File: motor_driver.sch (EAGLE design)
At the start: 43 parts, among them IC1 LM2936DT-5.0, Q1 BC849SMD, Q10 IRLML5203, Q11 BC849SMD, Q2 BC849SMD, Q3 BC849SMD, Q4 BC849SMD, Q5 BC849SMD, Q6 BC849SMD, Q7 IRLML5203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

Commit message: changed resistors in m1, m2 drivers
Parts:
- R11, R12, R13, R14: device rcl:R-EU_R0603 -> rcl:R-EU_R2512
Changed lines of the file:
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@@
 <?xml version="1.0" encoding="utf-8"?>
 <!DOCTYPE eagle SYSTEM "eagle.dtd">
-<eagle version="7.1.0">
+<eagle version="7.2.0">
 <drawing>
 <settings>
@@
 <grid distance="0.1" unitdist="inch" unit="inch" style="lines" multiple="1" display="no" altdistance="0.01" altunitdist="inch" altunit="inch"/>
 <layers>
-<layer number="1" name="Top" color="4" fill="1" visible="no" active="no"/>
-<layer number="16" name="Bottom" color="1" fill="1" visible="no" active="no"/>
-<layer number="17" name="Pads" color="2" fill="1" visible="no" active="no"/>
-<layer number="18" name="Vias" color="2" fill="1" visible="no" active="no"/>
-<layer number="19" name="Unrouted" color="6" fill="1" visible="no" active="no"/>
-<layer number="20" name="Dimension" color="15" fill="1" visible="no" active="no"/>
-<layer number="21" name="tPlace" color="7" fill="1" visible="no" active="no"/>
-<layer number="22" name="bPlace" color="7" fill="1" visible="no" active="no"/>
-<layer number="23" name="tOrigins" color="15" fill="1" visible="no" active="no"/>
-<layer number="24" name="bOrigins" color="15" fill="1" visible="no" active="no"/>
-<layer number="25" name="tNames" color="7" fill="1" visible="no" active="no"/>
-<layer number="26" name="bNames" color="7" fill="1" visible="no" active="no"/>
-<layer number="27" name="tValues" color="7" fill="1" visible="no" active="no"/>
-<layer number="28" name="bValues" color="7" fill="1" visible="no" active="no"/>
+<layer number="1" name="Top" color="4" fill="1" visible="yes" active="no"/>
+<layer number="16" name="Bottom" color="1" fill="1" visible="yes" active="no"/>
+<layer number="17" name="Pads" color="2" fill="1" visible="yes" active="no"/>
+<layer number="18" name="Vias" color="2" fill="1" visible="yes" active="no"/>
+<layer number="19" name="Unrouted" color="6" fill="1" visible="yes" active="no"/>
+<layer number="20" name="Dimension" color="15" fill="1" visible="yes" active="no"/>
+<layer number="21" name="tPlace" color="7" fill="1" visible="yes" active="no"/>
+<layer number="22" name="bPlace" color="7" fill="1" visible="yes" active="no"/>
+<layer number="23" name="tOrigins" color="15" fill="1" visible="yes" active="no"/>
+<layer number="24" name="bOrigins" color="15" fill="1" visible="yes" active="no"/>
+<layer number="25" name="tNames" color="7" fill="1" visible="yes" active="no"/>
+<layer number="26" name="bNames" color="7" fill="1" visible="yes" active="no"/>
+<layer number="27" name="tValues" color="7" fill="1" visible="yes" active="no"/>
+<layer number="28" name="bValues" color="7" fill="1" visible="yes" active="no"/>
 <layer number="29" name="tStop" color="7" fill="3" visible="no" active="no"/>
 <layer number="30" name="bStop" color="7" fill="6" visible="no" active="no"/>
@@
 <layer number="35" name="tGlue" color="7" fill="4" visible="no" active="no"/>
 <layer number="36" name="bGlue" color="7" fill="5" visible="no" active="no"/>
-<layer number="37" name="tTest" color="7" fill="1" visible="no" active="no"/>
-<layer number="38" name="bTest" color="7" fill="1" visible="no" active="no"/>
+<layer number="37" name="tTest" color="7" fill="1" visible="yes" active="no"/>
+<layer number="38" name="bTest" color="7" fill="1" visible="yes" active="no"/>
 <layer number="39" name="tKeepout" color="4" fill="11" visible="no" active="no"/>
 <layer number="40" name="bKeepout" color="1" fill="11" visible="no" active="no"/>
@@
 <layer number="44" name="Drills" color="7" fill="1" visible="no" active="no"/>
 <layer number="45" name="Holes" color="7" fill="1" visible="no" active="no"/>
-<layer number="46" name="Milling" color="3" fill="1" visible="no" active="no"/>
-<layer number="47" name="Measures" color="7" fill="1" visible="no" active="no"/>
-<layer number="48" name="Document" color="7" fill="1" visible="no" active="no"/>
-<layer number="49" name="Reference" color="7" fill="1" visible="no" active="no"/>
-<layer number="51" name="tDocu" color="7" fill="1" visible="no" active="no"/>
-<layer number="52" name="bDocu" color="7" fill="1" visible="no" active="no"/>
+<layer number="46" name="Milling" color="3" fill="1" visible="yes" active="no"/>
+<layer number="47" name="Measures" color="7" fill="1" visible="yes" active="no"/>
+<layer number="48" name="Document" color="7" fill="1" visible="yes" active="no"/>
+<layer number="49" name="Reference" color="7" fill="1" visible="yes" active="no"/>
+<layer number="51" name="tDocu" color="7" fill="1" visible="yes" active="no"/>
+<layer number="52" name="bDocu" color="7" fill="1" visible="yes" active="no"/>
 <layer number="90" name="Modules" color="5" fill="1" visible="yes" active="yes"/>
 <layer number="91" name="Nets" color="2" fill="1" visible="yes" active="yes"/>
@@
 <part name="R10" library="rcl" deviceset="R-EU_" device="R0603" value="100k"/>
 <part name="R4" library="rcl" deviceset="R-EU_" device="R0603" value="10k"/>
-<part name="R14" library="rcl" deviceset="R-EU_" device="R0603" value="10"/>
-<part name="R12" library="rcl" deviceset="R-EU_" device="R0603" value="10"/>
+<part name="R14" library="rcl" deviceset="R-EU_" device="R2512" value="10"/>
+<part name="R12" library="rcl" deviceset="R-EU_" device="R2512" value="10"/>
 <part name="SUPPLY10" library="supply2" deviceset="VDD" device=""/>
 <part name="GND4" library="supply1" deviceset="GND" device=""/>
@@
 <part name="R9" library="rcl" deviceset="R-EU_" device="R0603" value="100k"/>
 <part name="R2" library="rcl" deviceset="R-EU_" device="R0603" value="10k"/>
-<part name="R13" library="rcl" deviceset="R-EU_" device="R0603" value="10"/>
-<part name="R11" library="rcl" deviceset="R-EU_" device="R0603" value="10"/>
+<part name="R13" library="rcl" deviceset="R-EU_" device="R2512" value="10"/>
+<part name="R11" library="rcl" deviceset="R-EU_" device="R2512" value="10"/>
 <part name="SUPPLY9" library="supply2" deviceset="VDD" device=""/>
 <part name="GND3" library="supply1" deviceset="GND" device=""/>

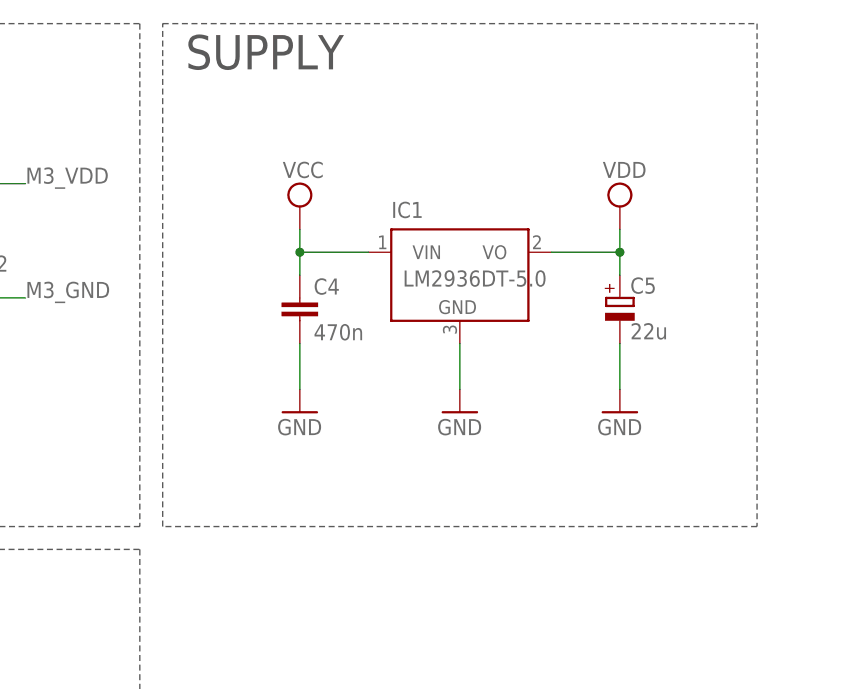
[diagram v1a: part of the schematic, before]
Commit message: added LED, added bom
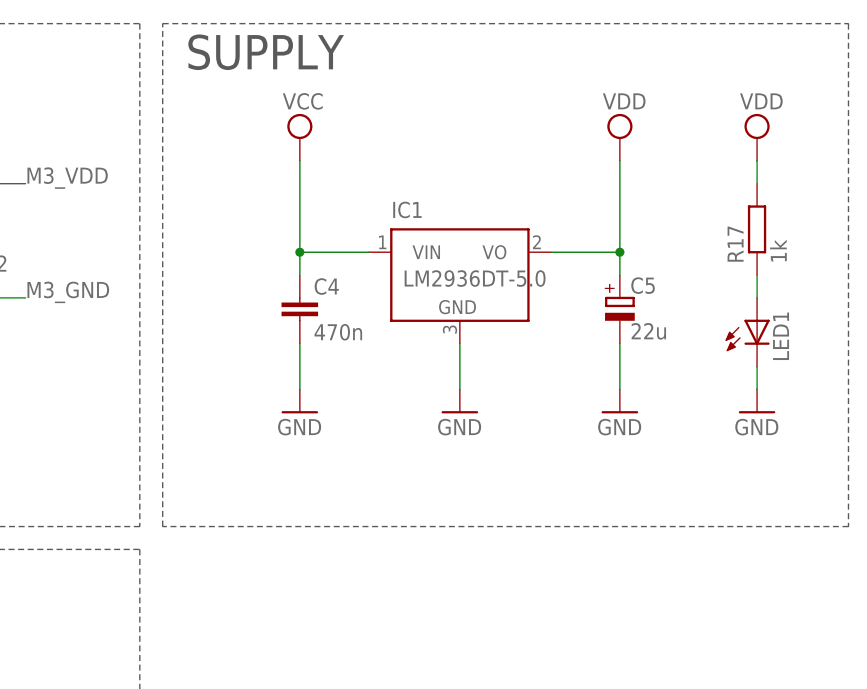
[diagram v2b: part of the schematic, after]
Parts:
- added LED1: (no value), led:LEDCHIPLED_0603
- added R17: 1k, rcl:R-EU_R0603
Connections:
- new net N$17: LED1.A, R17.1
- net GND: now also LED1.C
- net VDD: now also R17.2
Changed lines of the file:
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@@
 <setting verticaltext="up"/>
 </settings>
-<grid distance="0.1" unitdist="inch" unit="inch" style="lines" multiple="1" display="no" altdistance="0.01" altunitdist="inch" altunit="inch"/>
+<grid distance="0.1" unitdist="inch" unit="inch" style="lines" multiple="1" display="yes" altdistance="0.01" altunitdist="inch" altunit="inch"/>
 <layers>
-<layer number="1" name="Top" color="4" fill="1" visible="yes" active="no"/>
-<layer number="16" name="Bottom" color="1" fill="1" visible="yes" active="no"/>
-<layer number="17" name="Pads" color="2" fill="1" visible="yes" active="no"/>
-<layer number="18" name="Vias" color="2" fill="1" visible="yes" active="no"/>
-<layer number="19" name="Unrouted" color="6" fill="1" visible="yes" active="no"/>
-<layer number="20" name="Dimension" color="15" fill="1" visible="yes" active="no"/>
-<layer number="21" name="tPlace" color="7" fill="1" visible="yes" active="no"/>
-<layer number="22" name="bPlace" color="7" fill="1" visible="yes" active="no"/>
-<layer number="23" name="tOrigins" color="15" fill="1" visible="yes" active="no"/>
-<layer number="24" name="bOrigins" color="15" fill="1" visible="yes" active="no"/>
-<layer number="25" name="tNames" color="7" fill="1" visible="yes" active="no"/>
-<layer number="26" name="bNames" color="7" fill="1" visible="yes" active="no"/>
-<layer number="27" name="tValues" color="7" fill="1" visible="yes" active="no"/>
-<layer number="28" name="bValues" color="7" fill="1" visible="yes" active="no"/>
+<layer number="1" name="Top" color="4" fill="1" visible="no" active="no"/>
+<layer number="16" name="Bottom" color="1" fill="1" visible="no" active="no"/>
+<layer number="17" name="Pads" color="2" fill="1" visible="no" active="no"/>
+<layer number="18" name="Vias" color="2" fill="1" visible="no" active="no"/>
+<layer number="19" name="Unrouted" color="6" fill="1" visible="no" active="no"/>
+<layer number="20" name="Dimension" color="15" fill="1" visible="no" active="no"/>
+<layer number="21" name="tPlace" color="7" fill="1" visible="no" active="no"/>
+<layer number="22" name="bPlace" color="7" fill="1" visible="no" active="no"/>
+<layer number="23" name="tOrigins" color="15" fill="1" visible="no" active="no"/>
+<layer number="24" name="bOrigins" color="15" fill="1" visible="no" active="no"/>
+<layer number="25" name="tNames" color="7" fill="1" visible="no" active="no"/>
+<layer number="26" name="bNames" color="7" fill="1" visible="no" active="no"/>
+<layer number="27" name="tValues" color="7" fill="1" visible="no" active="no"/>
+<layer number="28" name="bValues" color="7" fill="1" visible="no" active="no"/>
 <layer number="29" name="tStop" color="7" fill="3" visible="no" active="no"/>
 <layer number="30" name="bStop" color="7" fill="6" visible="no" active="no"/>
@@
 <layer number="35" name="tGlue" color="7" fill="4" visible="no" active="no"/>
 <layer number="36" name="bGlue" color="7" fill="5" visible="no" active="no"/>
-<layer number="37" name="tTest" color="7" fill="1" visible="yes" active="no"/>
-<layer number="38" name="bTest" color="7" fill="1" visible="yes" active="no"/>
+<layer number="37" name="tTest" color="7" fill="1" visible="no" active="no"/>
+<layer number="38" name="bTest" color="7" fill="1" visible="no" active="no"/>
 <layer number="39" name="tKeepout" color="4" fill="11" visible="no" active="no"/>
 <layer number="40" name="bKeepout" color="1" fill="11" visible="no" active="no"/>
@@
 <layer number="44" name="Drills" color="7" fill="1" visible="no" active="no"/>
 <layer number="45" name="Holes" color="7" fill="1" visible="no" active="no"/>
-<layer number="46" name="Milling" color="3" fill="1" visible="yes" active="no"/>
-<layer number="47" name="Measures" color="7" fill="1" visible="yes" active="no"/>
-<layer number="48" name="Document" color="7" fill="1" visible="yes" active="no"/>
-<layer number="49" name="Reference" color="7" fill="1" visible="yes" active="no"/>
-<layer number="51" name="tDocu" color="7" fill="1" visible="yes" active="no"/>
-<layer number="52" name="bDocu" color="7" fill="1" visible="yes" active="no"/>
+<layer number="46" name="Milling" color="3" fill="1" visible="no" active="no"/>
+<layer number="47" name="Measures" color="7" fill="1" visible="no" active="no"/>
+<layer number="48" name="Document" color="7" fill="1" visible="no" active="no"/>
+<layer number="49" name="Reference" color="7" fill="1" visible="no" active="no"/>
+<layer number="51" name="tDocu" color="7" fill="1" visible="no" active="no"/>
+<layer number="52" name="bDocu" color="7" fill="1" visible="no" active="no"/>
 <layer number="90" name="Modules" color="5" fill="1" visible="yes" active="yes"/>
 <layer number="91" name="Nets" color="2" fill="1" visible="yes" active="yes"/>
@@
 <part name="C4" library="rcl" deviceset="C-EU" device="C0805" value="470n"/>
 <part name="C5" library="rcl" deviceset="CPOL-EU" device="150CLZ-1014" value="22u"/>
+<part name="LED1" library="led" deviceset="LED" device="CHIPLED_0603"/>
+<part name="R17" library="rcl" deviceset="R-EU_" device="R0603" value="1k"/>
+<part name="SUPPLY16" library="supply2" deviceset="VDD" device=""/>
+<part name="GND16" library="supply1" deviceset="GND" device=""/>
 </parts>
 <sheets>
@@
 <wire x1="185.42" y1="0" x2="114.3" y2="0" width="0.1524" layer="97" style="longdash"/>
 <wire x1="114.3" y1="0" x2="114.3" y2="106.68" width="0.1524" layer="97" style="longdash"/>
-<wire x1="187.96" y1="165.1" x2="254" y2="165.1" width="0.1524" layer="97" style="longdash"/>
-<wire x1="254" y1="165.1" x2="254" y2="109.22" width="0.1524" layer="97" style="longdash"/>
-<wire x1="254" y1="109.22" x2="187.96" y2="109.22" width="0.1524" layer="97" style="longdash"/>
+<wire x1="187.96" y1="165.1" x2="264.16" y2="165.1" width="0.1524" layer="97" style="longdash"/>
+<wire x1="264.16" y1="165.1" x2="264.16" y2="109.22" width="0.1524" layer="97" style="longdash"/>
+<wire x1="264.16" y1="109.22" x2="187.96" y2="109.22" width="0.1524" layer="97" style="longdash"/>
 <wire x1="187.96" y1="109.22" x2="187.96" y2="165.1" width="0.1524" layer="97" style="longdash"/>
 <text x="116.84" y="101.6" size="3.81" layer="97">CONN</text>
@@
 <instance part="C3" gate="G$1" x="165.1" y="142.24"/>
 <instance part="IC1" gate="G$1" x="220.98" y="137.16"/>
-<instance part="SUPPLY14" gate="G$1" x="203.2" y="144.78"/>
+<instance part="SUPPLY14" gate="G$1" x="203.2" y="152.4"/>
 <instance part="GND14" gate="1" x="220.98" y="121.92"/>
-<instance part="SUPPLY15" gate="G$1" x="238.76" y="144.78"/>
+<instance part="SUPPLY15" gate="G$1" x="238.76" y="152.4"/>
 <instance part="GND13" gate="1" x="203.2" y="121.92"/>
 <instance part="GND15" gate="1" x="238.76" y="121.92"/>
 <instance part="C4" gate="G$1" x="203.2" y="134.62"/>
 <instance part="C5" gate="G$1" x="238.76" y="134.62"/>
+<instance part="LED1" gate="G$1" x="254" y="132.08"/>
+<instance part="R17" gate="G$1" x="254" y="142.24" smashed="yes" rot="R90">
+<attribute name="NAME" x="252.5014" y="138.43" size="1.778" layer="95" rot="R90"/>
+<attribute name="VALUE" x="257.302" y="138.43" size="1.778" layer="96" rot="R90"/>
+</instance>
+<instance part="SUPPLY16" gate="G$1" x="254" y="152.4"/>
+<instance part="GND16" gate="1" x="254" y="121.92"/>
 </instances>
 <busses>
@@
 <pinref part="GND15" gate="1" pin="GND"/>
 <wire x1="238.76" y1="129.54" x2="238.76" y2="124.46" width="0.1524" layer="91"/>
+</segment>
+<segment>
+<pinref part="LED1" gate="G$1" pin="C"/>
+<pinref part="GND16" gate="1" pin="GND"/>
+<wire x1="254" y1="127" x2="254" y2="124.46" width="0.1524" layer="91"/>
 </segment>
 </net>
@@
 <wire x1="231.14" y1="139.7" x2="238.76" y2="139.7" width="0.1524" layer="91"/>
 <pinref part="SUPPLY15" gate="G$1" pin="VDD"/>
-<wire x1="238.76" y1="139.7" x2="238.76" y2="142.24" width="0.1524" layer="91"/>
+<wire x1="238.76" y1="139.7" x2="238.76" y2="149.86" width="0.1524" layer="91"/>
 <pinref part="C5" gate="G$1" pin="+"/>
 <wire x1="238.76" y1="139.7" x2="238.76" y2="137.16" width="0.1524" layer="91"/>
 <junction x="238.76" y="139.7"/>
+</segment>
+<segment>
+<pinref part="SUPPLY16" gate="G$1" pin="VDD"/>
+<pinref part="R17" gate="G$1" pin="2"/>
+<wire x1="254" y1="149.86" x2="254" y2="147.32" width="0.1524" layer="91"/>
 </segment>
 </net>
@@
 <segment>
 <pinref part="SUPPLY14" gate="G$1" pin="VCC"/>
-<wire x1="203.2" y1="142.24" x2="203.2" y2="139.7" width="0.1524" layer="91"/>
+<wire x1="203.2" y1="149.86" x2="203.2" y2="139.7" width="0.1524" layer="91"/>
 <pinref part="IC1" gate="G$1" pin="VIN"/>
 <wire x1="203.2" y1="139.7" x2="210.82" y2="139.7" width="0.1524" layer="91"/>
@@
 </segment>
 </net>
+<net name="N$17" class="0">
+<segment>
+<pinref part="R17" gate="G$1" pin="1"/>
+<pinref part="LED1" gate="G$1" pin="A"/>
+<wire x1="254" y1="137.16" x2="254" y2="134.62" width="0.1524" layer="91"/>
+</segment>
+</net>
